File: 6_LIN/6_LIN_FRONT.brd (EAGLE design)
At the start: 71.5 x 24 mm, 3 parts

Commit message: Cleanup, front with lib elements
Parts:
- removed E$1: (no value), AllSerialv2:PANEL
- removed E$2: (no value), AllSerialv2:RIA_AKL182-03
- removed E$3: (no value), AllSerialv2:LSTB-02-1
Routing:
- removed copper zone on layer 16, net S$1
- removed copper zone on layer 16, net S$2
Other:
- outline, holes or cut-outs redrawn
- board text added: "AllSerial LIN"
- board text removed: "AllSerial - LIN v1.2 46/18"
- board text removed: "LIN"

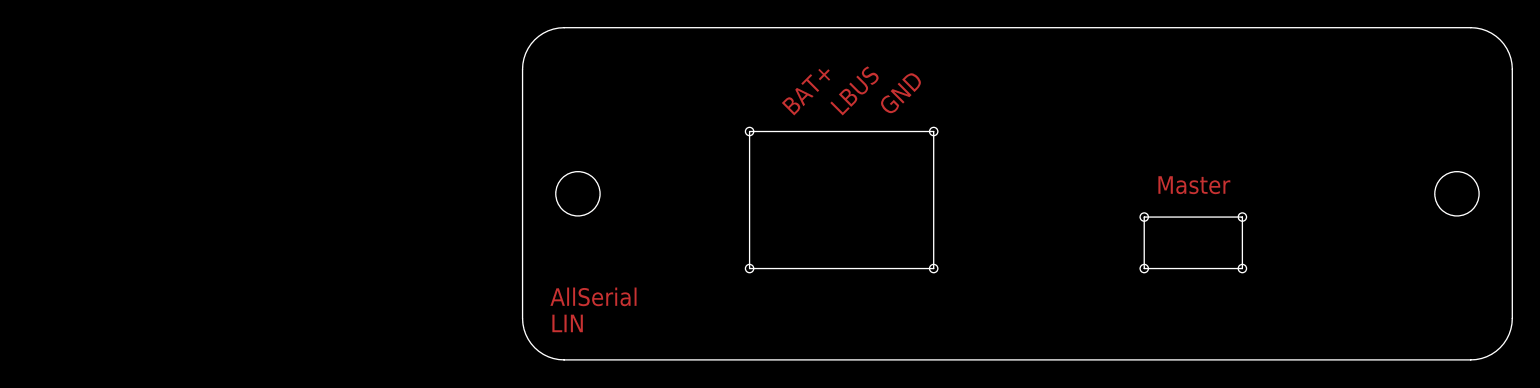
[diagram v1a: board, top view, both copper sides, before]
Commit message: pro mini layout corrected
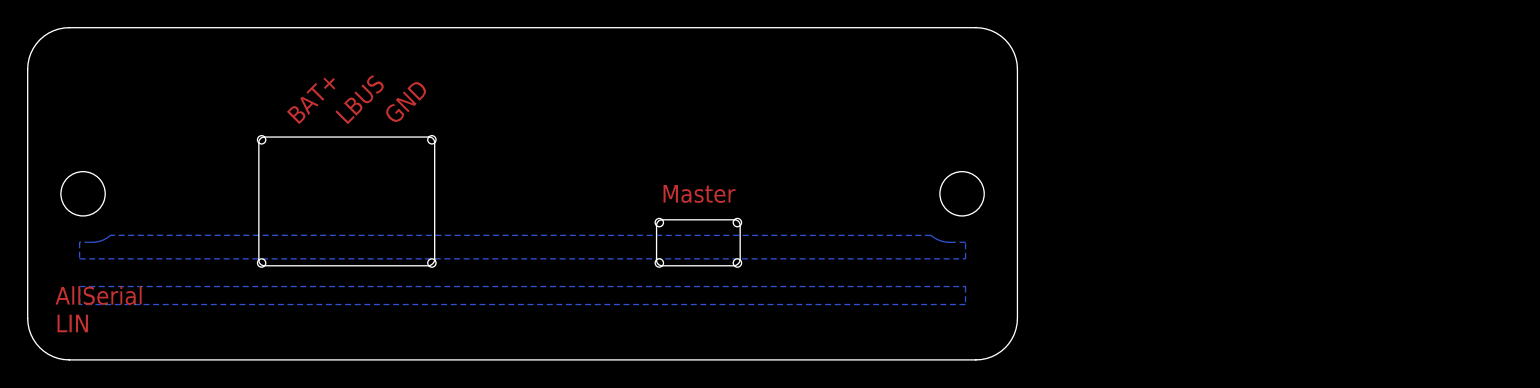
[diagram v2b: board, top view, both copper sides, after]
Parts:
- added E$1: (no value), AllSerialv2:PANEL
- added E$2: (no value), AllSerialv2:RIA_AKL182-03
- added E$3: (no value), AllSerialv2:LSTB-02-1
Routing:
- added copper zone on layer 16, net S$1
- added copper zone on layer 16, net S$2
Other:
- outline, holes or cut-outs redrawn
- board text added: "AllSerial - LIN v1.2 46/18"
- board text added: "LIN"
- board text removed: "AllSerial LIN"
